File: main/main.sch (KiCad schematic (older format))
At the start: 35 parts, among them J1 Conn_01x10_Female, J2 USB_B, J3 AVR-ISP-6, J4 Micro SD Card, Q1 2N7002, Q2 BSS84, U1 ATmega1284P-PU, U2 AMS1117, U3 MCP2221A-I_SL, U4 TXB0104D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

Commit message: annotated schematic
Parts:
- renumbered Reset to SW1
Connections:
- net GND: now also U5.8 (OE)
- net at Q2.3 (D), R5.2: no longer U5.8 (OE)
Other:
- note added: "3.3V Voltage Regulator"
- note added: "AVR Programmer SPI Transceiver\n"
- note added: "Bulk and Balance Caps"
- note added: "Processor\n"
- note added: "Reset Network"
- note added: "SD Card"
- note added: "SD Card SPI Transceiver"
- note added: "Terminal UART USB Translator"
- moved on the sheet: C1, C10, C2, C3, C4, C5, C6, C7, C8, C9, H1, H2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

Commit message: designed V2
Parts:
- removed C10, C6, C8: 1u, Capacitor_SMD:C_1206_3216Metric, symbol Device:C
- removed C5, C9: 10u, Capacitor_SMD:C_1206_3216Metric, symbol Device:C
- removed J1: Conn_01x10_Female, Connector_PinSocket_2.54mm:PinSocket_1x10_P2.54mm_Vertical, symbol Connector:Conn_01x10_Female
- removed J2: USB_B, Connector_USB:USB_B_OST_USB-B1HSxx_Horizontal, symbol Connector:USB_B
- removed J3: AVR-ISP-6, Connector_IDC:IDC-Header_2x03_P2.54mm_Vertical, symbol Connector:AVR-ISP-6
- removed J4: Micro SD Card, footprints:5027740891, symbol Connector:Micro_SD_Card
- removed Q1: 2N7002, Package_TO_SOT_SMD:SOT-23, symbol Transistor_FET:2N7002
- removed Q2: BSS84, Package_TO_SOT_SMD:SOT-23, symbol Transistor_FET:BSS84
- removed R3: 100, Resistor_SMD:R_1210_3225Metric, symbol Device:R
- removed R4, R5, R6, R7, R8, R9: 100k, Resistor_SMD:R_1210_3225Metric, symbol Device:R
- removed U2: AMS1117, Package_TO_SOT_SMD:SOT-223-3_TabPin2, symbol Regulator_Linear:AMS1117
- removed U3: MCP2221A-I_SL, Package_SO:SOIC-14_3.9x8.7mm_P1.27mm, symbol MCP2221A-I_SL:MCP2221A-I_SL
- removed U4, U5: TXB0104D, Package_SO:TSSOP-14_4.4x5mm_P0.65mm, symbol Logic_LevelTranslator:TXB0104D
- added AVR-ISP-5V1: AVR-ISP-6, Connector_IDC:IDC-Header_2x03_P2.54mm_Vertical, symbol Connector:AVR-ISP-6
- added J1: Conn_01x18_Female, Connector_PinHeader_2.54mm:PinHeader_1x18_P2.54mm_Vertical, symbol Connector:Conn_01x18_Female
- added POWER1: USB_B, Connector_USB:USB_B_OST_USB-B1HSxx_Horizontal, symbol Connector:USB_B
- added SD1: Conn_01x06_Female, Connector_PinHeader_2.54mm:PinHeader_1x06_P2.54mm_Vertical, symbol Connector:Conn_01x06_Female
- added TERM1: Conn_01x05_Female, Connector_PinSocket_2.54mm:PinSocket_1x05_P2.54mm_Vertical, symbol Connector:Conn_01x05_Female
- R2: value 100 -> 100k
- RESET1: renamed from SW1; footprint Button_Switch_SMD:SW_SPST_B3SL-1002P -> Button_Switch_THT:SW_PUSH_6mm_H4.3mm
- U1: footprint Package_QFP:TQFP-44_10x10mm_P0.8mm -> Package_DIP:DIP-40_W15.24mm_Socket
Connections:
- net +5V: now also R2.1, AVR-ISP-5V1.2 (VCC), J1.17 (Pin_17), POWER1.1 (VBUS), SD1.5 (Pin_5), TERM1.5 (Pin_5)
- net CS: now also R2.2, U1.14 (PD0), SD1.1 (Pin_1); no longer U1.40 (PA0)
- net GND: now also AVR-ISP-5V1.6 (GND), J1.18 (Pin_18), POWER1.4 (GND), POWER1.5 (Shield), SD1.6 (Pin_6), TERM1.1 (Pin_1)
- net MISO: now also AVR-ISP-5V1.1 (MISO), SD1.4 (Pin_4)
- net MOSI: now also AVR-ISP-5V1.4 (MOSI), SD1.3 (Pin_3)
- net RST: now also AVR-ISP-5V1.5 (~RST)
- net SCK: now also AVR-ISP-5V1.3 (SCK), SD1.2 (Pin_2)
- net URX: now also TERM1.3 (Pin_3)
- net UTX: now also TERM1.2 (Pin_2)
- net at U1.22 (PC0): now also J1.16 (Pin_16)
- net at U1.23 (PC1): now also J1.15 (Pin_15)
- net at U1.24 (PC2): now also J1.14 (Pin_14)
- net at U1.25 (PC3): now also J1.13 (Pin_13)
- net at U1.26 (PC4): now also J1.12 (Pin_12)
- net at U1.27 (PC5): now also J1.11 (Pin_11)
- net at U1.28 (PC6): now also J1.10 (Pin_10)
- net at U1.29 (PC7): now also J1.9 (Pin_9)
- net GP7: now reaches U1.33 (PA7)
- net GP7: now also J1.8 (Pin_8)
- net GP6: now reaches U1.34 (PA6)
- net GP6: now also J1.7 (Pin_7)
- net GP5: now reaches U1.35 (PA5)
- net GP5: now also J1.6 (Pin_6)
- net GP4: now reaches U1.36 (PA4)
- net GP4: now also J1.5 (Pin_5)
- net GP3: now reaches U1.37 (PA3)
- net GP3: now also J1.4 (Pin_4)
- net GP2: now reaches U1.38 (PA2)
- net GP2: now also J1.3 (Pin_3)
- net SD_EN renamed GP1
- net GP1: now also J1.2 (Pin_2); no longer R2.2
- new net GP0: J1.1 (Pin_1), U1.40 (PA0)
- no-connect marks 28 -> 15
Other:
- note added: "Programmer\n"
- note added: "SD-Card\n"
- note added: "USB to TTL adaptor"
- note removed: "3.3V Voltage Regulator"
- note removed: "AVR Programmer SPI Transceiver\n"
- note removed: "SD Card"
- note removed: "SD Card SPI Transceiver"
- note removed: "SPI Mode\n\n1. NC\n2. CS\n3. MOSI\n4. VDD\n5. SCK\n6. VSS\n7. MISO\n8. NC\n"
- note removed: "Terminal UART USB Translator"
- note removed: "cs is active low, ergo pullup\n"
- note removed: "gpio and i2c are not used.\n"
- note removed: "programmer config does not matter.\nonly common ground."
- moved on the sheet: H1, H2, H3, H4, R1, RESET1, U1

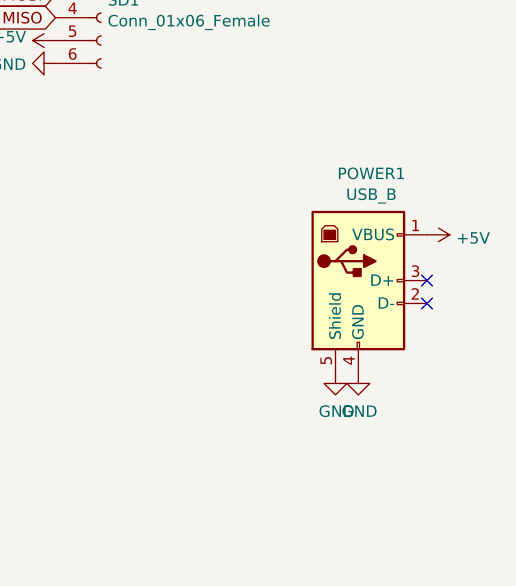
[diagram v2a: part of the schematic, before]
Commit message: removed unnecessary usb-b port
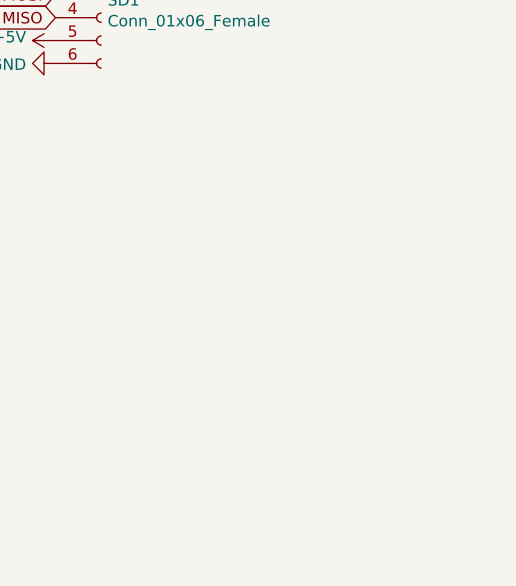
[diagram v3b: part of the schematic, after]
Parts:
- removed POWER1: USB_B, Connector_USB:USB_B_OST_USB-B1HSxx_Horizontal, symbol Connector:USB_B
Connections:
- no-connect marks 15 -> 13
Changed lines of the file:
@@
 Text Notes 5350 4200 0    138  ~ 0
 USB to TTL adaptor
-$Comp
-L Connector:USB_B POWER1
-U 1 1 694B1DCC
-P 9625 5700
-F 0 "POWER1" H 9682 6167 50  0000 C CNN
-F 1 "USB_B" H 9682 6076 50  0000 C CNN
-F 2 "Connector_USB:USB_B_OST_USB-B1HSxx_Horizontal" H 9775 5650 50  0001 C CNN
-F 3 " ~" H 9775 5650 50  0001 C CNN
-	1    9625 5700
-	1    0    0    -1
-$EndComp
-$Comp
-L power:GND #PWR0108
-U 1 1 694B2484
-P 9625 6100
-F 0 "#PWR0108" H 9625 5850 50  0001 C CNN
-F 1 "GND" H 9630 5927 50  0000 C CNN
-F 2 "" H 9625 6100 50  0001 C CNN
-F 3 "" H 9625 6100 50  0001 C CNN
-	1    9625 6100
-	1    0    0    -1
-$EndComp
-$Comp
-L power:GND #PWR0109
-U 1 1 694B261E
-P 9525 6100
-F 0 "#PWR0109" H 9525 5850 50  0001 C CNN
-F 1 "GND" H 9530 5927 50  0000 C CNN
-F 2 "" H 9525 6100 50  0001 C CNN
-F 3 "" H 9525 6100 50  0001 C CNN
-	1    9525 6100
-	1    0    0    -1
-$EndComp
-$Comp
-L power:+5V #PWR0110
-U 1 1 694B2BB7
-P 9925 5500
-F 0 "#PWR0110" H 9925 5350 50  0001 C CNN
-F 1 "+5V" V 9940 5628 50  0000 L CNN
-F 2 "" H 9925 5500 50  0001 C CNN
-F 3 "" H 9925 5500 50  0001 C CNN
-	1    9925 5500
-	0    1    1    0
-$EndComp
-NoConn ~ 9925 5700
-NoConn ~ 9925 5800
 Wire Wire Line
 	3450 3600 4275 3600
